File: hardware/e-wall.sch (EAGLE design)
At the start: 1 part

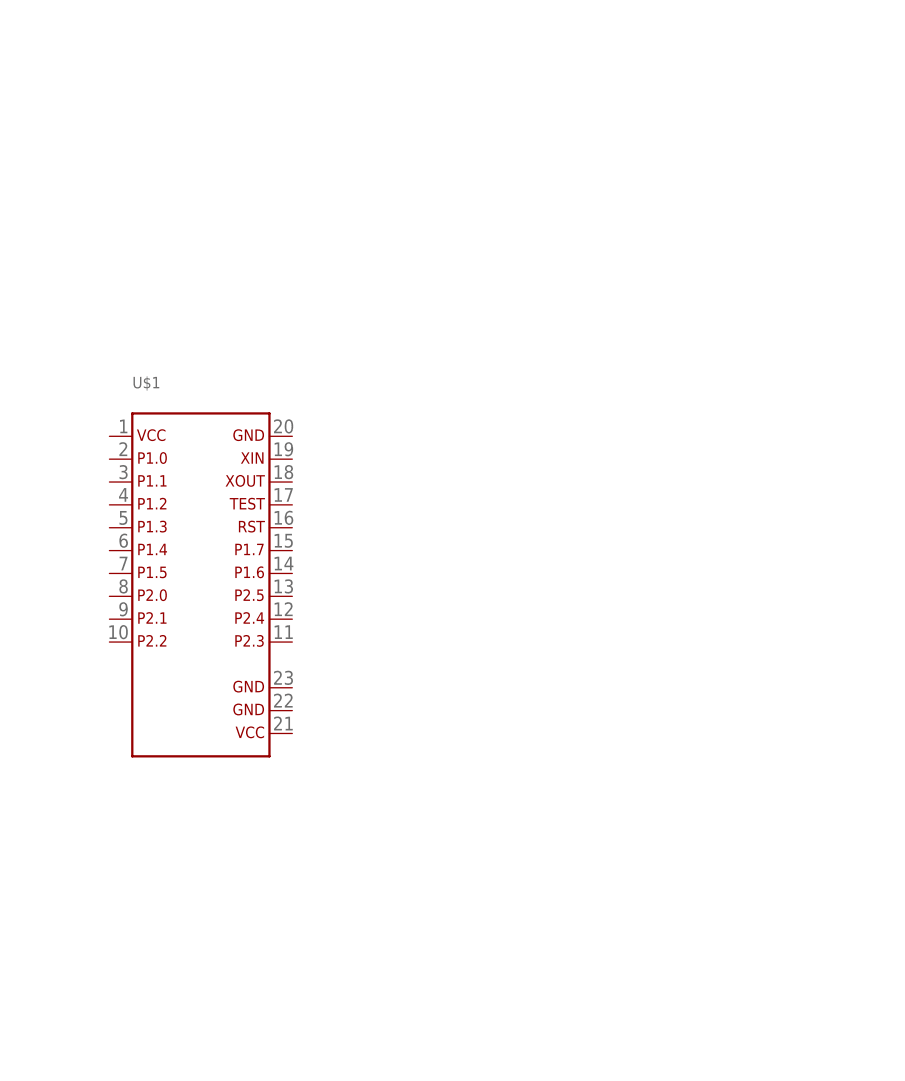
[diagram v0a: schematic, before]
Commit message: Schieberegister für LEDs und Lüfter
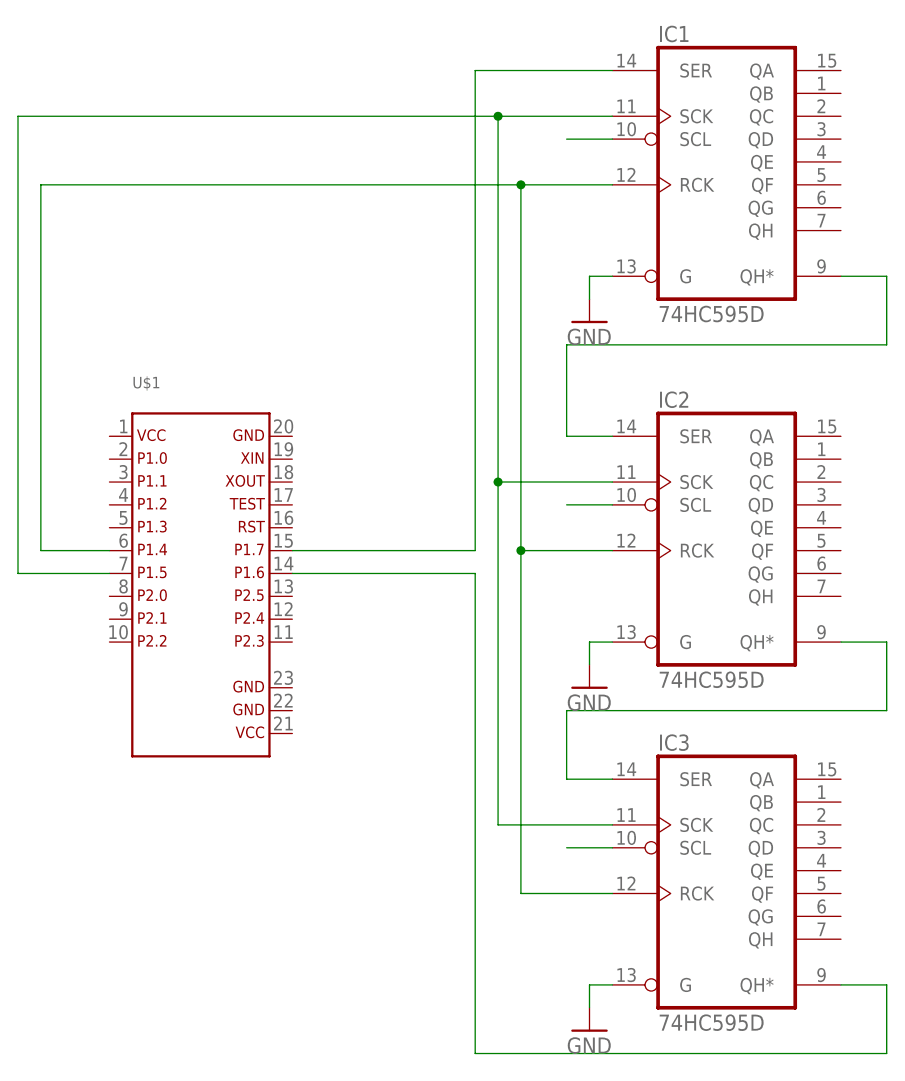
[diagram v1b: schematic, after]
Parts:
- added IC1, IC2, IC3: 74HC595D, 74xx-eu:74HC595D
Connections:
- new net GND: IC1A.G, IC2A.G, IC3A.G
- new net N$1: IC1A.QH*, IC2A.SER
- new net N$2: IC2A.QH*, IC3A.SER
- new net N$3: IC1A.SER, U$1.15
- new net N$4: IC1A.SCK, IC2A.SCK, IC3A.SCK, U$1.7
- new net N$5: IC1A.RCK, IC2A.RCK, IC3A.RCK, U$1.6
- new net N$6: IC3A.SCL
- new net N$7: IC2A.SCL
- new net N$8: IC1A.SCL
- new net N$9: IC3A.QH*, U$1.14
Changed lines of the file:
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@@
 <parts>
 <part name="U$1" library="msp430launchpad" deviceset="MSP430LAUNCHPAD_FULL" device=""/>
+<part name="IC1" library="74xx-eu" deviceset="74*595" device="D" technology="HC"/>
+<part name="IC2" library="74xx-eu" deviceset="74*595" device="D" technology="HC"/>
+<part name="IC3" library="74xx-eu" deviceset="74*595" device="D" technology="HC"/>
+<part name="GND1" library="supply1" deviceset="GND" device=""/>
+<part name="GND2" library="supply1" deviceset="GND" device=""/>
+<part name="GND3" library="supply1" deviceset="GND" device=""/>
 </parts>
 <sheets>
@@
 <instances>
 <instance part="U$1" gate="G$1" x="78.74" y="60.96"/>
+<instance part="IC1" gate="A" x="137.16" y="104.14"/>
+<instance part="IC2" gate="A" x="137.16" y="63.5"/>
+<instance part="IC3" gate="A" x="137.16" y="25.4"/>
+<instance part="GND1" gate="1" x="121.92" y="86.36"/>
+<instance part="GND2" gate="1" x="121.92" y="45.72"/>
+<instance part="GND3" gate="1" x="121.92" y="7.62"/>
 </instances>
 <busses>
 </busses>
 <nets>
+<net name="N$1" class="0">
+<segment>
+<pinref part="IC1" gate="A" pin="QH*"/>
+<wire x1="149.86" y1="91.44" x2="154.94" y2="91.44" width="0.1524" layer="91"/>
+<wire x1="154.94" y1="91.44" x2="154.94" y2="83.82" width="0.1524" layer="91"/>
+<wire x1="154.94" y1="83.82" x2="119.38" y2="83.82" width="0.1524" layer="91"/>
+<wire x1="119.38" y1="83.82" x2="119.38" y2="73.66" width="0.1524" layer="91"/>
+<pinref part="IC2" gate="A" pin="SER"/>
+<wire x1="119.38" y1="73.66" x2="124.46" y2="73.66" width="0.1524" layer="91"/>
+</segment>
+</net>
+<net name="N$2" class="0">
+<segment>
+<pinref part="IC2" gate="A" pin="QH*"/>
+<wire x1="149.86" y1="50.8" x2="154.94" y2="50.8" width="0.1524" layer="91"/>
+<wire x1="154.94" y1="50.8" x2="154.94" y2="43.18" width="0.1524" layer="91"/>
+<wire x1="154.94" y1="43.18" x2="119.38" y2="43.18" width="0.1524" layer="91"/>
+<wire x1="119.38" y1="43.18" x2="119.38" y2="35.56" width="0.1524" layer="91"/>
+<pinref part="IC3" gate="A" pin="SER"/>
+<wire x1="119.38" y1="35.56" x2="124.46" y2="35.56" width="0.1524" layer="91"/>
+</segment>
+</net>
+<net name="N$3" class="0">
+<segment>
+<pinref part="U$1" gate="G$1" pin="15"/>
+<wire x1="88.9" y1="60.96" x2="109.22" y2="60.96" width="0.1524" layer="91"/>
+<wire x1="109.22" y1="60.96" x2="109.22" y2="114.3" width="0.1524" layer="91"/>
+<pinref part="IC1" gate="A" pin="SER"/>
+<wire x1="109.22" y1="114.3" x2="124.46" y2="114.3" width="0.1524" layer="91"/>
+</segment>
+</net>
+<net name="GND" class="0">
+<segment>
+<pinref part="IC3" gate="A" pin="G"/>
+<pinref part="GND3" gate="1" pin="GND"/>
+<wire x1="124.46" y1="12.7" x2="121.92" y2="12.7" width="0.1524" layer="91"/>
+<wire x1="121.92" y1="12.7" x2="121.92" y2="10.16" width="0.1524" layer="91"/>
+</segment>
+<segment>
+<pinref part="IC2" gate="A" pin="G"/>
+<pinref part="GND2" gate="1" pin="GND"/>
+<wire x1="124.46" y1="50.8" x2="121.92" y2="50.8" width="0.1524" layer="91"/>
+<wire x1="121.92" y1="50.8" x2="121.92" y2="48.26" width="0.1524" layer="91"/>
+</segment>
+<segment>
+<pinref part="IC1" gate="A" pin="G"/>
+<pinref part="GND1" gate="1" pin="GND"/>
+<wire x1="124.46" y1="91.44" x2="121.92" y2="91.44" width="0.1524" layer="91"/>
+<wire x1="121.92" y1="91.44" x2="121.92" y2="88.9" width="0.1524" layer="91"/>
+</segment>
+</net>
+<net name="N$4" class="0">
+<segment>
+<pinref part="IC1" gate="A" pin="SCK"/>
+<wire x1="124.46" y1="109.22" x2="111.76" y2="109.22" width="0.1524" layer="91"/>
+<wire x1="111.76" y1="109.22" x2="111.76" y2="68.58" width="0.1524" layer="91"/>
+<pinref part="IC3" gate="A" pin="SCK"/>
+<wire x1="111.76" y1="68.58" x2="111.76" y2="30.48" width="0.1524" layer="91"/>
+<wire x1="111.76" y1="30.48" x2="124.46" y2="30.48" width="0.1524" layer="91"/>
+<pinref part="IC2" gate="A" pin="SCK"/>
+<wire x1="124.46" y1="68.58" x2="111.76" y2="68.58" width="0.1524" layer="91"/>
+<junction x="111.76" y="68.58"/>
+<junction x="111.76" y="109.22"/>
+<wire x1="111.76" y1="109.22" x2="58.42" y2="109.22" width="0.1524" layer="91"/>
+<wire x1="58.42" y1="109.22" x2="58.42" y2="58.42" width="0.1524" layer="91"/>
+<pinref part="U$1" gate="G$1" pin="7"/>
+<wire x1="58.42" y1="58.42" x2="68.58" y2="58.42" width="0.1524" layer="91"/>
+</segment>
+</net>
+<net name="N$5" class="0">
+<segment>
+<pinref part="IC1" gate="A" pin="RCK"/>
+<wire x1="124.46" y1="101.6" x2="114.3" y2="101.6" width="0.1524" layer="91"/>
+<wire x1="114.3" y1="101.6" x2="114.3" y2="60.96" width="0.1524" layer="91"/>
+<pinref part="IC3" gate="A" pin="RCK"/>
+<wire x1="114.3" y1="60.96" x2="114.3" y2="22.86" width="0.1524" layer="91"/>
+<wire x1="114.3" y1="22.86" x2="124.46" y2="22.86" width="0.1524" layer="91"/>
+<pinref part="IC2" gate="A" pin="RCK"/>
+<wire x1="124.46" y1="60.96" x2="114.3" y2="60.96" width="0.1524" layer="91"/>
+<junction x="114.3" y="60.96"/>
+<junction x="114.3" y="101.6"/>
+<wire x1="114.3" y1="101.6" x2="60.96" y2="101.6" width="0.1524" layer="91"/>
+<wire x1="60.96" y1="101.6" x2="60.96" y2="60.96" width="0.1524" layer="91"/>
+<pinref part="U$1" gate="G$1" pin="6"/>
+<wire x1="60.96" y1="60.96" x2="68.58" y2="60.96" width="0.1524" layer="91"/>
+</segment>
+</net>
+<net name="N$6" class="0">
+<segment>
+<pinref part="IC3" gate="A" pin="SCL"/>
+<wire x1="124.46" y1="27.94" x2="119.38" y2="27.94" width="0.1524" layer="91"/>
+</segment>
+</net>
+<net name="N$7" class="0">
+<segment>
+<pinref part="IC2" gate="A" pin="SCL"/>
+<wire x1="124.46" y1="66.04" x2="119.38" y2="66.04" width="0.1524" layer="91"/>
+</segment>
+</net>
+<net name="N$8" class="0">
+<segment>
+<pinref part="IC1" gate="A" pin="SCL"/>
+<wire x1="124.46" y1="106.68" x2="119.38" y2="106.68" width="0.1524" layer="91"/>
+</segment>
+</net>
+<net name="N$9" class="0">
+<segment>
+<pinref part="IC3" gate="A" pin="QH*"/>
+<wire x1="149.86" y1="12.7" x2="154.94" y2="12.7" width="0.1524" layer="91"/>
+<wire x1="154.94" y1="12.7" x2="154.94" y2="5.08" width="0.1524" layer="91"/>
+<wire x1="154.94" y1="5.08" x2="109.22" y2="5.08" width="0.1524" layer="91"/>
+<wire x1="109.22" y1="5.08" x2="109.22" y2="58.42" width="0.1524" layer="91"/>
+<pinref part="U$1" gate="G$1" pin="14"/>
+<wire x1="109.22" y1="58.42" x2="88.9" y2="58.42" width="0.1524" layer="91"/>
+</segment>
+</net>
 </nets>
 </sheet>

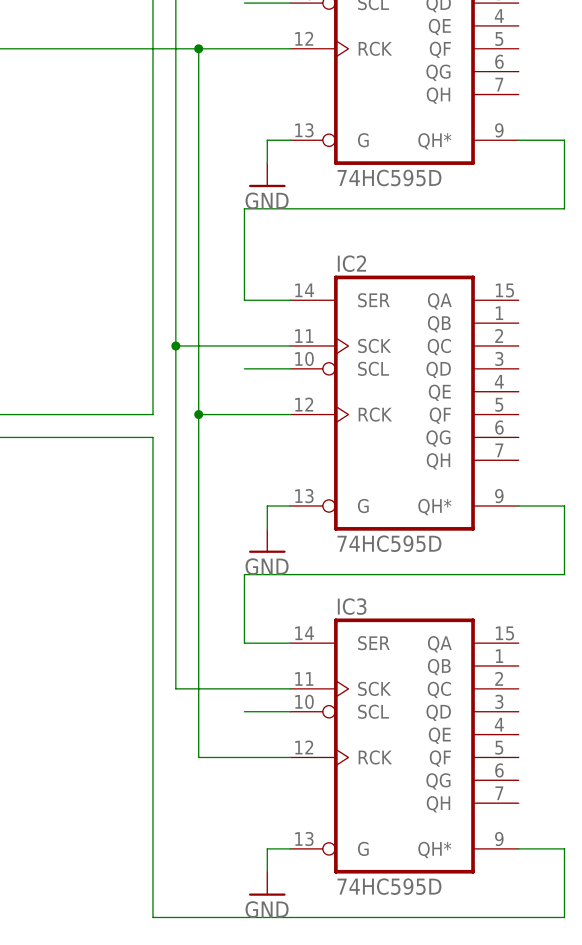
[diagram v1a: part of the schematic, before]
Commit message: Technologie der Schieberegister von 74HC zu 74HCT geändert
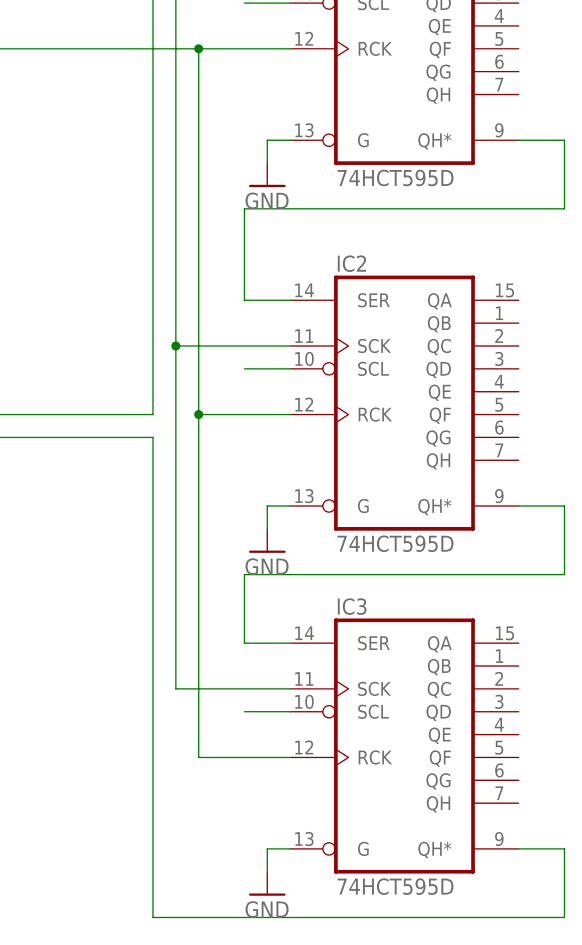
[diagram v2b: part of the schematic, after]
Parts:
- IC1, IC2, IC3: value 74HC595D -> 74HCT595D; device 74xx-eu:74HC595D -> 74xx-eu:74HCT595D
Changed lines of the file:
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@@
 <parts>
 <part name="U$1" library="msp430launchpad" deviceset="MSP430LAUNCHPAD_FULL" device=""/>
-<part name="IC1" library="74xx-eu" deviceset="74*595" device="D" technology="HC"/>
-<part name="IC2" library="74xx-eu" deviceset="74*595" device="D" technology="HC"/>
-<part name="IC3" library="74xx-eu" deviceset="74*595" device="D" technology="HC"/>
+<part name="IC1" library="74xx-eu" deviceset="74*595" device="D" technology="HCT" value="74HCT595D"/>
+<part name="IC2" library="74xx-eu" deviceset="74*595" device="D" technology="HCT" value="74HCT595D"/>
+<part name="IC3" library="74xx-eu" deviceset="74*595" device="D" technology="HCT" value="74HCT595D"/>
 <part name="GND1" library="supply1" deviceset="GND" device=""/>
 <part name="GND2" library="supply1" deviceset="GND" device=""/>

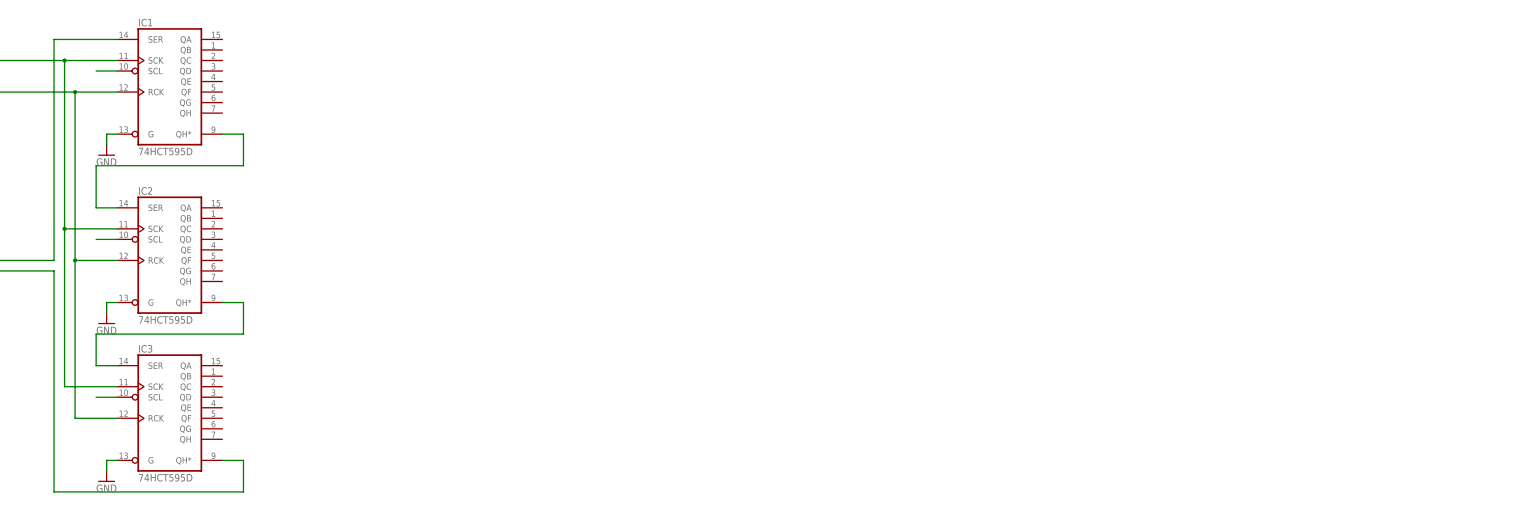
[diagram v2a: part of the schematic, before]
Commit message: Treiber für LED und Lüfter
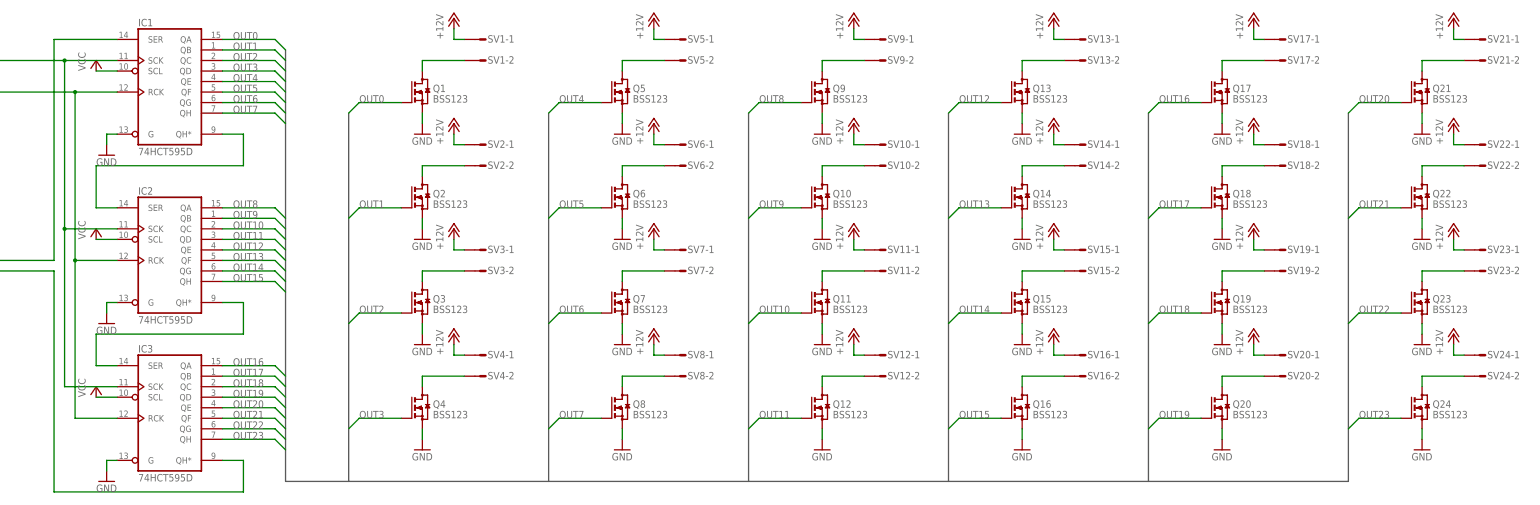
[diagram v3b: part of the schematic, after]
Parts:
- added Q1, Q10, Q11, Q12, Q13, Q14, Q15, Q16, Q17, Q18, Q19, Q2, Q20, Q21, Q22, Q23, Q24, Q3, Q4, Q5, Q6, Q7, Q8, Q9: BSS123, transistor-small-signal:BSS123
- added SV1, SV10, SV11, SV12, SV13, SV14, SV15, SV16, SV17, SV18, SV19, SV2, SV20, SV21, SV22, SV23, SV24, SV3, SV4, SV5, SV6, SV7, SV8, SV9: (no value), con-amp-mt:L02P
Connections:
- new net +12V: SV1-1.S, SV10-1.S, SV11-1.S, SV12-1.S, SV13-1.S, SV14-1.S, SV15-1.S, SV16-1.S, SV17-1.S, SV18-1.S, SV19-1.S, SV2-1.S, SV20-1.S, SV21-1.S, SV22-1.S, SV23-1.S, SV24-1.S, SV3-1.S, SV4-1.S, SV5-1.S, SV6-1.S, SV7-1.S, SV8-1.S, SV9-1.S
- new net N$10: Q1.D, SV1-2.S
- new net N$11: Q8.D, SV8-2.S
- new net N$12: Q7.D, SV7-2.S
- new net N$13: Q6.D, SV6-2.S
- new net N$14: Q5.D, SV5-2.S
- new net N$15: Q12.D, SV12-2.S
- new net N$16: Q11.D, SV11-2.S
- new net N$17: Q10.D, SV10-2.S
- new net N$18: Q9.D, SV9-2.S
- new net N$19: Q16.D, SV16-2.S
- new net N$20: Q15.D, SV15-2.S
- new net N$21: Q14.D, SV14-2.S
- new net N$22: Q13.D, SV13-2.S
- new net N$23: Q20.D, SV20-2.S
- new net N$24: Q19.D, SV19-2.S
- new net N$25: Q18.D, SV18-2.S
- new net N$26: Q17.D, SV17-2.S
- new net N$27: Q24.D, SV24-2.S
- new net N$28: Q23.D, SV23-2.S
- new net N$29: Q22.D, SV22-2.S
- new net N$30: Q21.D, SV21-2.S
- new net OUT0: IC1A.QA, Q1.G
- new net OUT1: IC1A.QB, Q2.G
- new net OUT10: IC2A.QC, Q11.G
- new net OUT11: IC2A.QD, Q12.G
- new net OUT12: IC2A.QE, Q13.G
- new net OUT13: IC2A.QF, Q14.G
- new net OUT14: IC2A.QG, Q15.G
- new net OUT15: IC2A.QH, Q16.G
- new net OUT16: IC3A.QA, Q17.G
- new net OUT17: IC3A.QB, Q18.G
- new net OUT18: IC3A.QC, Q19.G
- new net OUT19: IC3A.QD, Q20.G
- new net OUT2: IC1A.QC, Q3.G
- new net OUT20: IC3A.QE, Q21.G
- new net OUT21: IC3A.QF, Q22.G
- new net OUT22: IC3A.QG, Q23.G
- new net OUT23: IC3A.QH, Q24.G
- new net OUT3: IC1A.QD, Q4.G
- new net OUT4: IC1A.QE, Q5.G
- new net OUT5: IC1A.QF, Q6.G
- new net OUT6: IC1A.QG, Q7.G
- new net OUT7: IC1A.QH, Q8.G
- new net OUT8: IC2A.QA, Q9.G
- new net OUT9: IC2A.QB, Q10.G
- new net VCC: IC1A.SCL, IC2A.SCL, IC3A.SCL
- net GND: now also Q1.S, Q10.S, Q11.S, Q12.S, Q13.S, Q14.S, Q15.S, Q16.S, Q17.S, Q18.S, Q19.S, Q2.S, Q20.S, Q21.S, Q22.S, Q23.S, Q24.S, Q3.S, Q4.S, Q5.S, Q6.S, Q7.S, Q8.S, Q9.S
- net N$6: now also Q4.D, SV4-2.S; no longer IC3A.SCL
- net N$7: now also Q3.D, SV3-2.S; no longer IC2A.SCL
- net N$8: now also Q2.D, SV2-2.S; no longer IC1A.SCL

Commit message: Blöcke angeschrieben
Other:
- note added: "Schieberegister"
- note added: "Treiber für LED"
- note added: "Treiber für Lüfter"
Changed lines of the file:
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@@
 <sheet>
 <plain>
+<wire x1="180.34" y1="0" x2="185.42" y2="-5.08" width="0.1524" layer="97" curve="90"/>
+<wire x1="185.42" y1="-5.08" x2="246.38" y2="-5.08" width="0.1524" layer="97"/>
+<wire x1="246.38" y1="-5.08" x2="251.46" y2="-10.16" width="0.1524" layer="97" curve="-90"/>
+<wire x1="251.46" y1="-10.16" x2="256.54" y2="-5.08" width="0.1524" layer="97" curve="-90"/>
+<wire x1="256.54" y1="-5.08" x2="317.5" y2="-5.08" width="0.1524" layer="97"/>
+<wire x1="317.5" y1="-5.08" x2="322.58" y2="0" width="0.1524" layer="97" curve="90"/>
+<wire x1="325.12" y1="0" x2="330.2" y2="-5.08" width="0.1524" layer="97" curve="90"/>
+<wire x1="330.2" y1="-5.08" x2="391.16" y2="-5.08" width="0.1524" layer="97"/>
+<wire x1="391.16" y1="-5.08" x2="396.24" y2="-10.16" width="0.1524" layer="97" curve="-90"/>
+<wire x1="396.24" y1="-10.16" x2="401.32" y2="-5.08" width="0.1524" layer="97" curve="-90"/>
+<wire x1="401.32" y1="-5.08" x2="462.28" y2="-5.08" width="0.1524" layer="97"/>
+<wire x1="462.28" y1="-5.08" x2="467.36" y2="0" width="0.1524" layer="97" curve="90"/>
+<text x="243.84" y="-15.24" size="1.778" layer="97">Treiber für LED</text>
+<text x="388.62" y="-15.24" size="1.778" layer="97">Treiber für Lüfter</text>
+<wire x1="165.1" y1="0" x2="160.02" y2="-5.08" width="0.1524" layer="97" curve="-90"/>
+<wire x1="160.02" y1="-5.08" x2="142.24" y2="-5.08" width="0.1524" layer="97"/>
+<wire x1="142.24" y1="-5.08" x2="137.16" y2="-10.16" width="0.1524" layer="97" curve="90"/>
+<wire x1="137.16" y1="-10.16" x2="132.08" y2="-5.08" width="0.1524" layer="97" curve="90"/>
+<wire x1="132.08" y1="-5.08" x2="114.3" y2="-5.08" width="0.1524" layer="97"/>
+<wire x1="114.3" y1="-5.08" x2="109.22" y2="0" width="0.1524" layer="97" curve="-90"/>
+<text x="129.54" y="-15.24" size="1.778" layer="97">Schieberegister</text>
 </plain>
 <instances>
